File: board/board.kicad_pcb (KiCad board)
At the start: 2 copper layers, 61 x 13 mm, 34 parts, among them J1 USB4105-GF-A, J2 100_digital_IO, J3 SWD_6_Pol_Needle, J4 100_digital_IO, U1 W25Q16JVUXIQ, U2 RP2040, U3 TLV743P, Y1 12MhZ

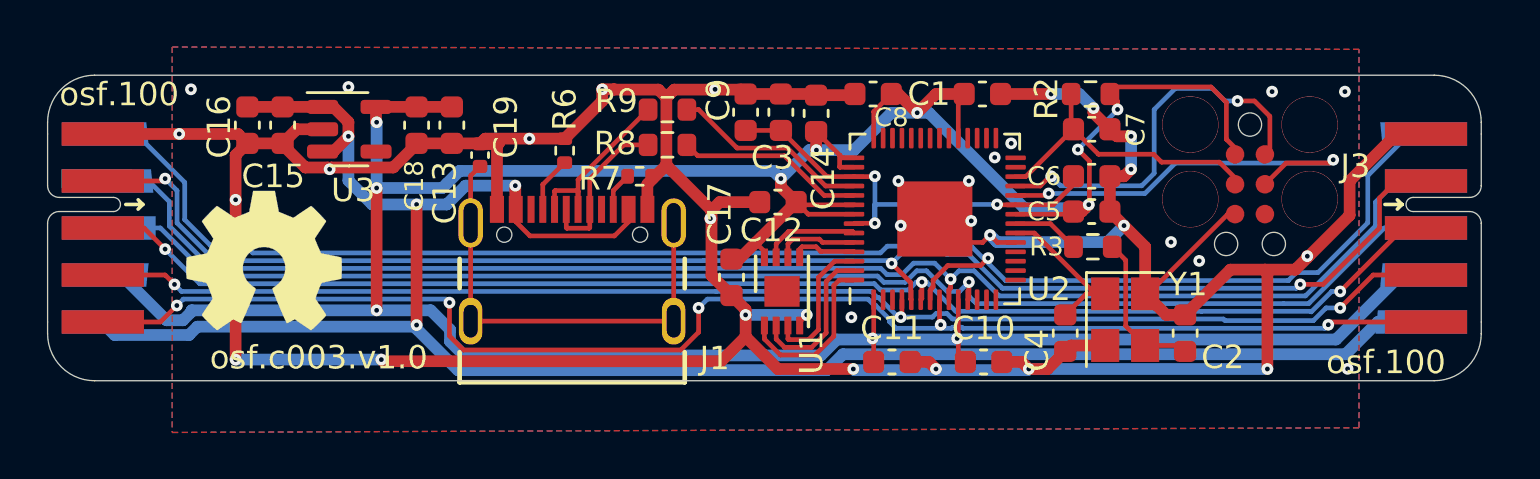
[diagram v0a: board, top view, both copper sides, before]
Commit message: added boot select button
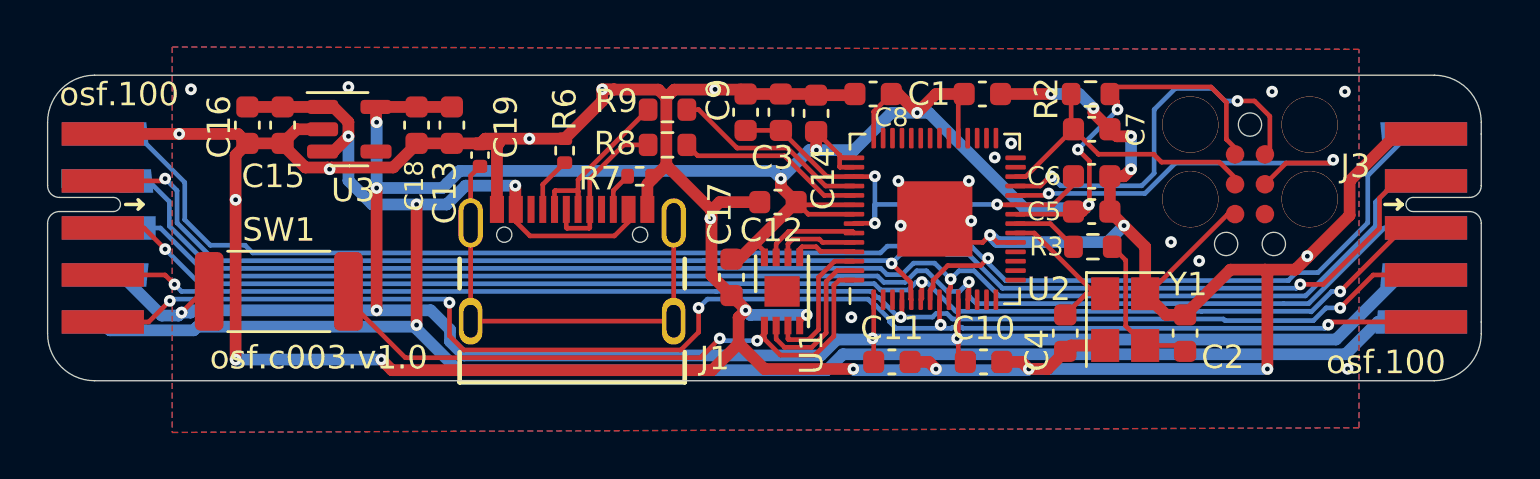
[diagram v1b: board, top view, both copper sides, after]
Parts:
- added SW1: PTS636 SK25J SMTR LFS, Resistor_SMD:R_2512_6332Metric, F.Cu at (149.8, 99.2)
- LOGO1: moved to B.Cu
- moved LOGO1 1.36 mm to (150.5, 98.3), turned to 180 degrees
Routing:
- net /rp2040/QPI_SS: track 7.25 -> 27.2 mm, vias 0 -> 2
- net +3V3: track 150.1 -> 151.5 mm, vias 11 -> 12
- net GND: track 171.6 -> 172.2 mm

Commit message: fixed boot select circuit
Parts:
- added R1: 1k, Resistor_SMD:R_0603_1608Metric, F.Cu at (155.7, 100.8)
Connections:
- SW1 pad 1: +3V3 -> GND
- SW1 pad 2: /rp2040/QPI_SS -> Net-(R1-Pad1)
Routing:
- net /rp2040/QPI_SS: track 27.2 -> 22.7 mm
- net Net-(R1-Pad1): track 0.00 -> 2.88 mm
- net +3V3: track 151.5 -> 149.9 mm, vias 12 -> 11
- net GND: track 172.2 -> 173.3 mm
